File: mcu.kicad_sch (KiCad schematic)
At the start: 45 parts, among them CN1 HX JN1.27-2X5 TP H4.9, J5 DM3CS-SF, SW3 TS-1088-AR02016, U1 STM32F405RGTx, U6 SS12D10G5, X1 X1E000210127000G

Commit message: footprints updated
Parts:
- C100: renamed from C34; footprint (none) -> Capacitor_SMD:C_0402_1005Metric
- C101: renamed from C35; footprint (none) -> Capacitor_SMD:C_0402_1005Metric
- C102: renamed from C36; footprint (none) -> Capacitor_SMD:C_0402_1005Metric
- C103: renamed from C28; footprint (none) -> Capacitor_SMD:C_0603_1608Metric
- C104: renamed from C23; footprint (none) -> Capacitor_SMD:C_0402_1005Metric
- C105: renamed from C24; footprint (none) -> Capacitor_SMD:C_0402_1005Metric
- C106: renamed from C25; footprint (none) -> Capacitor_SMD:C_0402_1005Metric
- C107: renamed from C33; footprint (none) -> Capacitor_SMD:C_0805_2012Metric
- C108: renamed from C26; footprint (none) -> Capacitor_SMD:C_0402_1005Metric
- C109: renamed from C32; footprint (none) -> Capacitor_SMD:C_0805_2012Metric
- C110: renamed from C27; footprint (none) -> Capacitor_SMD:C_0402_1005Metric
- C111: renamed from C37; footprint (none) -> Capacitor_SMD:C_0402_1005Metric
- C112: renamed from C29; footprint (none) -> Capacitor_SMD:C_0402_1005Metric
- C113: renamed from C39; footprint (none) -> Capacitor_SMD:C_0603_1608Metric
- C114: renamed from C30; footprint (none) -> Capacitor_SMD:C_0603_1608Metric
- C115: renamed from C41; footprint (none) -> Capacitor_SMD:C_0603_1608Metric
- C116: renamed from C31; footprint (none) -> Capacitor_SMD:C_0603_1608Metric
- C117: renamed from C38; footprint (none) -> Capacitor_SMD:C_0402_1005Metric
- C118: renamed from C40; footprint (none) -> Capacitor_SMD:C_0603_1608Metric
- D100: renamed from D5; footprint (none) -> LED_SMD:LED_0402_1005Metric
- D101: renamed from D2; footprint (none) -> LED_SMD:LED_0402_1005Metric
- D102: renamed from D3; footprint (none) -> LED_SMD:LED_0402_1005Metric
- D103: renamed from D4; footprint (none) -> LED_SMD:LED_0402_1005Metric
- FB100: renamed from FB2; footprint (none) -> Inductor_SMD:L_0805_2012Metric
- L100: renamed from L2; footprint (none) -> Inductor_SMD:L_0402_1005Metric
- R100: renamed from R11; footprint (none) -> Resistor_SMD:R_0402_1005Metric
- R101: renamed from R12; footprint (none) -> Resistor_SMD:R_0402_1005Metric
- R102: renamed from R16; footprint (none) -> Resistor_SMD:R_0402_1005Metric
- R103: renamed from R17; footprint (none) -> Resistor_SMD:R_0402_1005Metric
- R104: renamed from R18; footprint (none) -> Resistor_SMD:R_0402_1005Metric
- R105: renamed from R19; footprint (none) -> Resistor_SMD:R_0402_1005Metric
- R106: renamed from R20; footprint (none) -> Resistor_SMD:R_0402_1005Metric
- R107: renamed from R21; footprint (none) -> Resistor_SMD:R_0402_1005Metric
- R108: renamed from R22; footprint (none) -> Resistor_SMD:R_0402_1005Metric
- R109: renamed from R23; footprint (none) -> Resistor_SMD:R_0402_1005Metric
- R110: renamed from R15; footprint (none) -> Resistor_SMD:R_0402_1005Metric
- R111: renamed from R14; footprint (none) -> Resistor_SMD:R_0402_1005Metric
- R112: renamed from R13; footprint (none) -> Resistor_SMD:R_0402_1005Metric
- SW_100: renamed from SW3; value TS-1088-AR02016 -> SW_RESET
- U100: renamed from U6; value SS12D10G5 -> SW_RUN
- renumbered CN1 to CN100, ER-OLEDM015-2W1 to ER-OLEDM015-2W100, J5 to J100, U1 to U101, X1 to X100
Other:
- note added: "BOOT SELECTION"
- note added: "CRYSTAL OSCILLATOR"
- note added: "DEBUG CONNECTOR"
- note added: "LEDS"
- note added: "OLED SCREEN"
- note added: "RESET"
- note added: "SD CARD"
- note added: "STM32F4"
- note added: "[1]MCU"
- note removed: "MCU"
- moved on the sheet: C100, C101, C102, C103, C104, C105, C106, C107, C108, C109, C110, C111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

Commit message: decoupling caps route
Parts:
- C116: footprint Capacitor_SMD:C_0603_1608Metric -> Capacitor_SMD:C_0402_1005Metric
- L100: footprint Inductor_SMD:L_0402_1005Metric -> Inductor_SMD:L_0603_1608Metric
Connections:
- net +3V3: now also U101.1 (VBAT), U101.19 (VDD), U101.32 (VDD), U101.48 (VDD), U101.64 (VDD)
- net GND: no longer U101.1 (VBAT), U101.19 (VDD), U101.32 (VDD), U101.48 (VDD), U101.64 (VDD)
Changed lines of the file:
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@@
 	)
 	(junction
-		(at 209.55 43.18)
-		(diameter 0)
-		(color 0 0 0 0)
-	)
-	(junction
 		(at 58.42 116.84)
 		(diameter 0)
@@
 	)
 	(junction
-		(at 184.15 43.18)
-		(diameter 0)
-		(color 0 0 0 0)
-	)
-	(junction
 		(at 63.5 116.84)
 		(diameter 0)
@@
 	)
 	(junction
+		(at 209.55 43.18)
+		(diameter 0)
+		(color 0 0 0 0)
+	)
+	(junction
 		(at 176.53 185.42)
 		(diameter 0)
@@
 	)
 	(junction
+		(at 184.15 30.48)
+		(diameter 0)
+		(color 0 0 0 0)
+	)
+	(junction
 		(at 171.45 30.48)
 		(diameter 0)
@@
 	(wire
 		(pts
+			(xy 209.55 43.18) (xy 209.55 30.48)
+		)
+		(stroke
+			(width 0)
+			(type default)
+		)
+	)
+	(wire
+		(pts
 			(xy 234.95 86.36) (xy 241.3 86.36)
 		)
@@
 	(wire
 		(pts
-			(xy 184.15 30.48) (xy 171.45 30.48)
+			(xy 171.45 30.48) (xy 184.15 30.48)
 		)
 		(stroke
@@
 	(wire
 		(pts
-			(xy 209.55 43.18) (xy 184.15 43.18)
-		)
-		(stroke
-			(width 0)
-			(type default)
-		)
-	)
-	(wire
-		(pts
 			(xy 138.43 205.74) (xy 157.48 205.74)
 		)
@@
 	(wire
 		(pts
+			(xy 184.15 30.48) (xy 209.55 30.48)
+		)
+		(stroke
+			(width 0)
+			(type default)
+		)
+	)
+	(wire
+		(pts
 			(xy 222.25 31.75) (xy 226.06 31.75)
 		)
@@
 			)
 		)
-		(property "Footprint" "Capacitor_SMD:C_0603_1608Metric"
+		(property "Footprint" "Capacitor_SMD:C_0402_1005Metric"
 			(at 285.4452 41.91 0)
 			(effects
@@
 			)
 		)
-		(property "Footprint" "Inductor_SMD:L_0402_1005Metric"
+		(property "Footprint" "Inductor_SMD:L_0603_1608Metric"
 			(at 273.05 31.75 0)
 			(effects

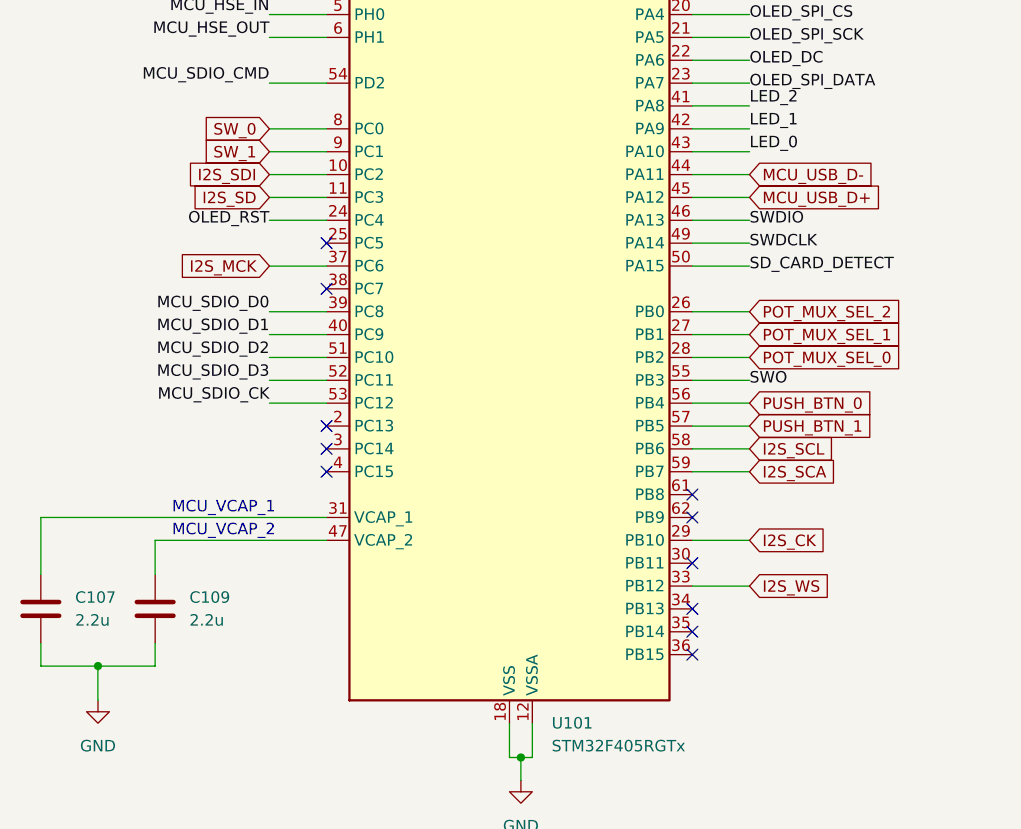
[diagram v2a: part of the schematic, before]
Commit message: codec placed
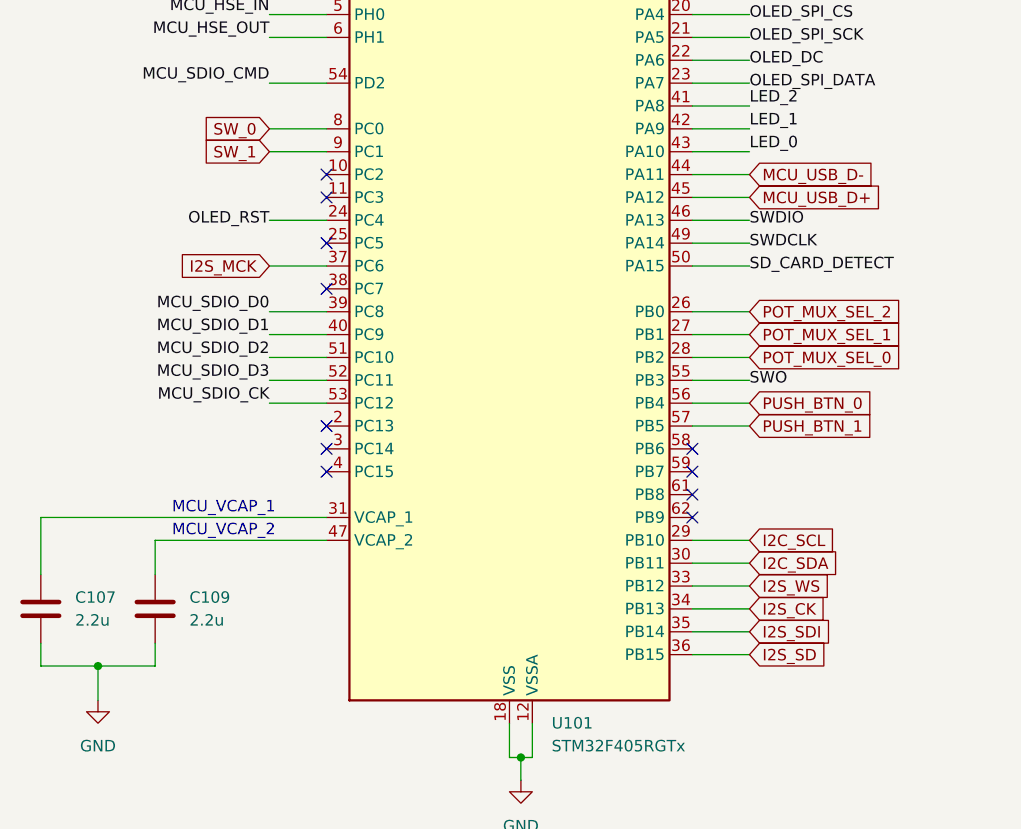
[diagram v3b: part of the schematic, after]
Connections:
- net I2S_CK: now also U101.34 (PB13); no longer U101.29 (PB10)
- net I2S_SD: now also U101.36 (PB15); no longer U101.11 (PC3)
- net I2S_SDI: now also U101.35 (PB14); no longer U101.10 (PC2)
- net I2C_SDA: now reaches U101.30 (PB11)
- net I2S_SCA: no longer names the net of U101.59 (PB7)
- net I2S_SCL: no longer names the net of U101.58 (PB6)
- new net I2C_SCL: U101.29 (PB10)
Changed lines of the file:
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@@
 	)
 	(no_connect
-		(at 234.95 132.08)
+		(at 194.31 81.28)
 	)
 	(no_connect
@@
 	)
 	(no_connect
-		(at 234.95 124.46)
-	)
-	(no_connect
-		(at 234.95 129.54)
-	)
-	(no_connect
 		(at 234.95 60.96)
 	)
@@
 	)
 	(no_connect
+		(at 194.31 83.82)
+	)
+	(no_connect
+		(at 234.95 111.76)
+	)
+	(no_connect
 		(at 234.95 116.84)
+	)
+	(no_connect
+		(at 234.95 114.3)
 	)
 	(no_connect
@@
 	)
 	(no_connect
-		(at 234.95 134.62)
-	)
-	(no_connect
 		(at 364.49 168.91)
 	)
@@
 	(wire
 		(pts
-			(xy 187.96 83.82) (xy 194.31 83.82)
-		)
-		(stroke
-			(width 0)
-			(type default)
-		)
-	)
-	(wire
-		(pts
 			(xy 252.73 180.34) (xy 245.11 180.34)
 		)
@@
 	(wire
 		(pts
-			(xy 234.95 114.3) (xy 241.3 114.3)
+			(xy 234.95 124.46) (xy 241.3 124.46)
 		)
 		(stroke
@@
 	(wire
 		(pts
+			(xy 234.95 132.08) (xy 241.3 132.08)
+		)
+		(stroke
+			(width 0)
+			(type default)
+		)
+	)
+	(wire
+		(pts
 			(xy 208.28 200.66) (xy 208.28 180.34)
 		)
@@
 	(wire
 		(pts
-			(xy 234.95 111.76) (xy 241.3 111.76)
+			(xy 234.95 121.92) (xy 241.3 121.92)
 		)
 		(stroke
@@
 	(wire
 		(pts
+			(xy 234.95 134.62) (xy 241.3 134.62)
+		)
+		(stroke
+			(width 0)
+			(type default)
+		)
+	)
+	(wire
+		(pts
 			(xy 284.48 27.94) (xy 284.48 31.75)
 		)
@@
 	(wire
 		(pts
-			(xy 234.95 121.92) (xy 241.3 121.92)
-		)
-		(stroke
-			(width 0)
-			(type default)
-		)
-	)
-	(wire
-		(pts
 			(xy 194.31 223.52) (xy 215.9 223.52)
 		)
@@
 	(wire
 		(pts
-			(xy 187.96 81.28) (xy 194.31 81.28)
-		)
-		(stroke
-			(width 0)
-			(type default)
-		)
-	)
-	(wire
-		(pts
 			(xy 187.96 101.6) (xy 194.31 101.6)
 		)
@@
 		(pts
 			(xy 234.95 73.66) (xy 241.3 73.66)
+		)
+		(stroke
+			(width 0)
+			(type default)
+		)
+	)
+	(wire
+		(pts
+			(xy 234.95 129.54) (xy 241.3 129.54)
 		)
 		(stroke
@@
 		)
 	)
+	(global_label "I2S_SDI"
+		(shape input)
+		(at 241.3 132.08 0)
+		(fields_autoplaced yes)
+		(effects
+			(font
+				(size 1.27 1.27)
+			)
+			(justify left)
+		)
+		(property "Intersheetrefs" "${INTERSHEET_REFS}"
+			(at 251.3609 132.08 0)
+			(effects
+				(font
+					(size 1.27 1.27)
+				)
+				(justify left)
+				(hide yes)
+			)
+		)
+	)
+	(global_label "I2S_SD"
+		(shape input)
+		(at 241.3 134.62 0)
+		(fields_autoplaced yes)
+		(effects
+			(font
+				(size 1.27 1.27)
+			)
+			(justify left)
+		)
+		(property "Intersheetrefs" "${INTERSHEET_REFS}"
+			(at 250.7561 134.62 0)
+			(effects
+				(font
+					(size 1.27 1.27)
+				)
+				(justify left)
+				(hide yes)
+			)
+		)
+	)
 	(global_label "SW_0"
 		(shape input)
@@
 		)
 	)
-	(global_label "I2S_SD"
-		(shape input)
-		(at 187.96 83.82 180)
-		(fields_autoplaced yes)
-		(effects
-			(font
-				(size 1.27 1.27)
-			)
-			(justify right)
-		)
-		(property "Intersheetrefs" "${INTERSHEET_REFS}"
-			(at 178.5039 83.82 0)
-			(effects
-				(font
-					(size 1.27 1.27)
-				)
-				(justify right)
-				(hide yes)
-			)
-		)
-	)
 	(global_label "POT_MUX_SEL_2"
 		(shape input)
@@
 		)
 	)
-	(global_label "I2S_SCL"
+	(global_label "I2C_SCL"
 		(shape input)
-		(at 241.3 111.76 0)
+		(at 241.3 121.92 0)
 		(fields_autoplaced yes)
 		(effects
@@
 		)
 		(property "Intersheetrefs" "${INTERSHEET_REFS}"
-			(at 251.7842 111.76 0)
+			(at 251.8447 121.92 0)
 			(effects
 				(font
@@
 	(global_label "I2S_CK"
 		(shape input)
-		(at 241.3 121.92 0)
+		(at 241.3 129.54 0)
 		(fields_autoplaced yes)
 		(effects
@@
 		)
 		(property "Intersheetrefs" "${INTERSHEET_REFS}"
-			(at 250.8166 121.92 0)
+			(at 250.8166 129.54 0)
 			(effects
 				(font
@@
 		)
 	)
-	(global_label "I2S_SCA"
+	(global_label "I2C_SDA"
 		(shape input)
-		(at 241.3 114.3 0)
+		(at 241.3 124.46 0)
 		(fields_autoplaced yes)
 		(effects
@@
 		)
 		(property "Intersheetrefs" "${INTERSHEET_REFS}"
-			(at 251.8447 114.3 0)
+			(at 251.9052 124.46 0)
 			(effects
 				(font
@@
 				(hide yes)
 			)
-		)
-	)
-	(global_label "I2S_SDI"
-		(shape input)
-		(at 187.96 81.28 180)
-		(fields_autoplaced yes)
-		(effects
-			(font
-				(size 1.27 1.27)
-			)
-			(justify right)
-		)
-		(property "Intersheetrefs" "${INTERSHEET_REFS}"
-			(at 177.8991 81.28 0)
-			(effects
-				(font
-					(size 1.27 1.27)
-				)
-				(justify right)
-				(hide yes)
-			)

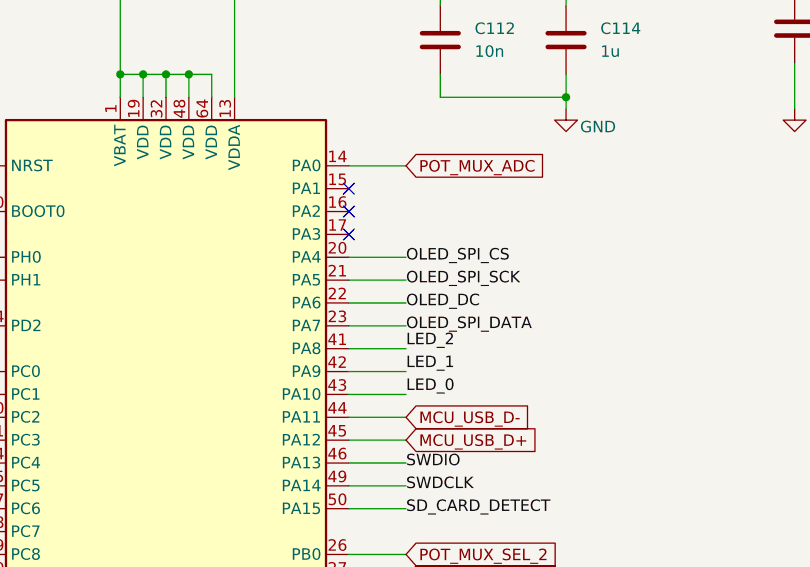
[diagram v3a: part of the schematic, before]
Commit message: control positioned
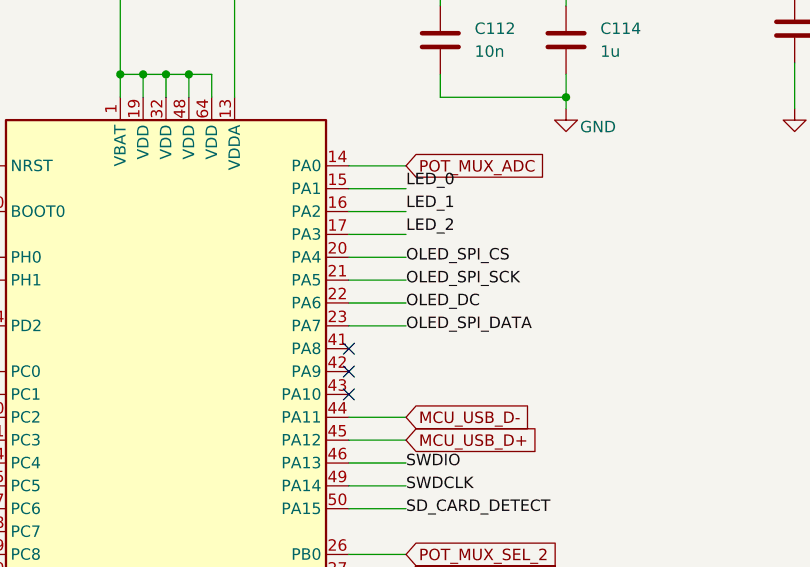
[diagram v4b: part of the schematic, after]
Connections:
- net LED_0: now also U101.15 (PA1); no longer U101.43 (PA10)
- net LED_1: now also U101.16 (PA2); no longer U101.42 (PA9)
- net LED_2: now also U101.17 (PA3); no longer U101.41 (PA8)
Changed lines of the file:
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@@
 	)
 	(no_connect
-		(at 234.95 58.42)
+		(at 234.95 76.2)
 	)
 	(no_connect
@@
 	)
 	(no_connect
-		(at 234.95 55.88)
+		(at 234.95 73.66)
 	)
 	(no_connect
@@
 	)
 	(no_connect
-		(at 234.95 60.96)
+		(at 234.95 78.74)
 	)
 	(no_connect
@@
 	(wire
 		(pts
-			(xy 234.95 76.2) (xy 241.3 76.2)
+			(xy 234.95 58.42) (xy 241.3 58.42)
 		)
 		(stroke
@@
 	(wire
 		(pts
-			(xy 234.95 78.74) (xy 241.3 78.74)
+			(xy 234.95 60.96) (xy 241.3 60.96)
 		)
 		(stroke
@@
 	(wire
 		(pts
-			(xy 234.95 73.66) (xy 241.3 73.66)
+			(xy 234.95 55.88) (xy 241.3 55.88)
 		)
 		(stroke
@@
 	)
 	(label "LED_1"
-		(at 241.3 76.2 0)
+		(at 241.3 58.42 0)
 		(effects
 			(font
@@
 		)
 	)
-	(label "LED_2"
-		(at 241.3 73.66 0)
+	(label "LED_0"
+		(at 241.3 55.88 0)
 		(effects
 			(font
@@
 		)
 	)
-	(label "LED_0"
-		(at 241.3 78.74 0)
-		(effects
-			(font
+	(label "LED_2"
+		(at 241.3 60.96 0)
+		(effects
+			(font

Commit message: updating names
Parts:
- added D104: RCLAMP0521P-N, Galerna:X1-DFN1006-2_L1.0-W0.6-P0.65-BI, symbol Galerna:RCLAMP0521P-N
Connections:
- net +3V3_SD: now also D104.2
- net GND: now also D104.1
- net I2C_SCL renamed CODEC_I2C_SCL
- net I2C_SDA renamed CODEC_I2C_SDA
- net I2S_CK renamed CODEC_I2S_CK
- net I2S_MCK renamed CODEC_I2S_MCK
- net I2S_SD renamed CODEC_I2S_SD
- net I2S_SDI renamed CODEC_I2S_SDI
- net I2S_WS renamed CODEC_I2S_WS
- net MCU_SDIO_CK renamed SDCARD_SDIO_CK
- net MCU_SDIO_CMD renamed SDCARD_SDIO_CMD
- net MCU_SDIO_D0 renamed SDCARD_SDIO_D0
- net MCU_SDIO_D1 renamed SDCARD_SDIO_D1
- net MCU_SDIO_D2 renamed SDCARD_SDIO_D2
- net MCU_SDIO_D3 renamed SDCARD_SDIO_D3
- net SD_CARD_DETECT renamed SDCARD_DETECT

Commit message: net classes added
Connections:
- net SWDCLK renamed SWD_CLK
- net SWDIO renamed SWD_IO
- net SWO renamed SWD_O
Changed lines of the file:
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@@
 		)
 	)
-	(label "SWO"
+	(label "SWD_O"
 		(at 369.57 166.37 0)
 		(effects
@@
 		)
 	)
-	(label "SWDCLK"
+	(label "SWD_CLK"
 		(at 369.57 163.83 0)
 		(effects
@@
 		)
 	)
-	(label "SWO"
+	(label "SWD_O"
 		(at 241.3 104.14 0)
 		(effects
@@
 		)
 	)
-	(label "SWDCLK"
+	(label "SWD_CLK"
 		(at 241.3 88.9 0)
 		(effects
@@
 		)
 	)
-	(label "SWDIO"
+	(label "SWD_IO"
 		(at 241.3 86.36 0)
 		(effects
@@
 		)
 	)
-	(label "SWDIO"
+	(label "SWD_IO"
 		(at 369.57 161.29 0)
 		(effects

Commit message: routing update
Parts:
- C116: footprint Capacitor_SMD:C_0402_1005Metric -> Capacitor_SMD:C_0603_1608Metric
- L100: footprint Inductor_SMD:L_0603_1608Metric -> Inductor_SMD:L_0402_1005Metric
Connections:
- net VDDA: now reaches C112.1, C114.1, L100.1, U101.13 (VDDA)
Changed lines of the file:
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@@
 		)
 	)
+	(label "VDDA"
+		(at 234.95 31.75 0)
+		(effects
+			(font
+				(size 1.27 1.27)
+			)
+			(justify left bottom)
+		)
+	)
 	(label "+3V3_SD"
 		(at 231.14 180.34 180)
@@
 	)
 	(global_label "CODEC_I2S_WS"
-		(shape input)
+		(shape output)
 		(at 241.3 127 0)
 		(fields_autoplaced yes)
@@
 	)
 	(global_label "CODEC_I2S_SD"
-		(shape input)
+		(shape output)
 		(at 241.3 134.62 0)
 		(fields_autoplaced yes)
@@
 	)
 	(global_label "POT_MUX_SEL_2"
-		(shape input)
+		(shape output)
 		(at 241.3 96.52 0)
 		(fields_autoplaced yes)
@@
 	)
 	(global_label "CODEC_I2C_SCL"
-		(shape input)
+		(shape output)
 		(at 241.3 121.92 0)
 		(fields_autoplaced yes)
@@
 	)
 	(global_label "CODEC_I2S_CK"
-		(shape input)
+		(shape output)
 		(at 241.3 129.54 0)
 		(fields_autoplaced yes)
@@
 	)
 	(global_label "CODEC_I2C_SDA"
-		(shape input)
+		(shape bidirectional)
 		(at 241.3 124.46 0)
 		(fields_autoplaced yes)
@@
 		)
 		(property "Intersheetrefs" "${INTERSHEET_REFS}"
-			(at 259.1623 124.46 0)
+			(at 260.2736 124.46 0)
 			(effects
 				(font
@@
 	)
 	(global_label "POT_MUX_SEL_1"
-		(shape input)
+		(shape output)
 		(at 241.3 99.06 0)
 		(fields_autoplaced yes)
@@
 	)
 	(global_label "POT_MUX_SEL_0"
-		(shape input)
+		(shape output)
 		(at 241.3 101.6 0)
 		(fields_autoplaced yes)
@@
 			)
 		)
-		(property "Footprint" "Capacitor_SMD:C_0402_1005Metric"
+		(property "Footprint" "Capacitor_SMD:C_0603_1608Metric"
 			(at 285.4452 41.91 0)
 			(effects
@@
 			)
 		)
-		(property "Footprint" "Inductor_SMD:L_0603_1608Metric"
+		(property "Footprint" "Inductor_SMD:L_0402_1005Metric"
 			(at 273.05 31.75 0)
 			(effects

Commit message: last update
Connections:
- net POT_MUX_SEL_0: now also U101.26 (PB0); no longer U101.28 (PB2)
- net POT_MUX_SEL_2: now also U101.28 (PB2); no longer U101.26 (PB0)
- net SW_0: now also U101.9 (PC1); no longer U101.8 (PC0)
- net SW_1: now also U101.8 (PC0); no longer U101.9 (PC1)
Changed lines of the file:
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@@
 		)
 	)
-	(global_label "SW_0"
+	(global_label "SW_1"
 		(shape input)
 		(at 187.96 76.2 180)
@@
 		)
 	)
-	(global_label "POT_MUX_SEL_2"
+	(global_label "POT_MUX_SEL_0"
 		(shape output)
 		(at 241.3 96.52 0)
@@
 		)
 	)
-	(global_label "SW_1"
+	(global_label "SW_0"
 		(shape input)
 		(at 187.96 78.74 180)
@@
 		)
 	)
-	(global_label "POT_MUX_SEL_0"
+	(global_label "POT_MUX_SEL_2"
 		(shape output)
 		(at 241.3 101.6 0)
